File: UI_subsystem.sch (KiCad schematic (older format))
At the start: 19 parts

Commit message: Added UI buttons, LEDs, Decoupling caps, MCU connections, and other good stuff.
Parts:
- added R?: 100, symbol Device:R_US
- added ZNP_BTN_?: SW_Push, symbol Switch:SW_Push
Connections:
- net labels added: GND, MCU_RESET, MCU_VDD
- net labels removed: +3V3, 3.3_TFT, GND8, PWR_LED
- wire segments 50 -> 57
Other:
- moved on the sheet: BB_BTN_301, BB_BTN_302, LED301, LED302, PWR301, R301, R302, R303, R304, R305, R306, R307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

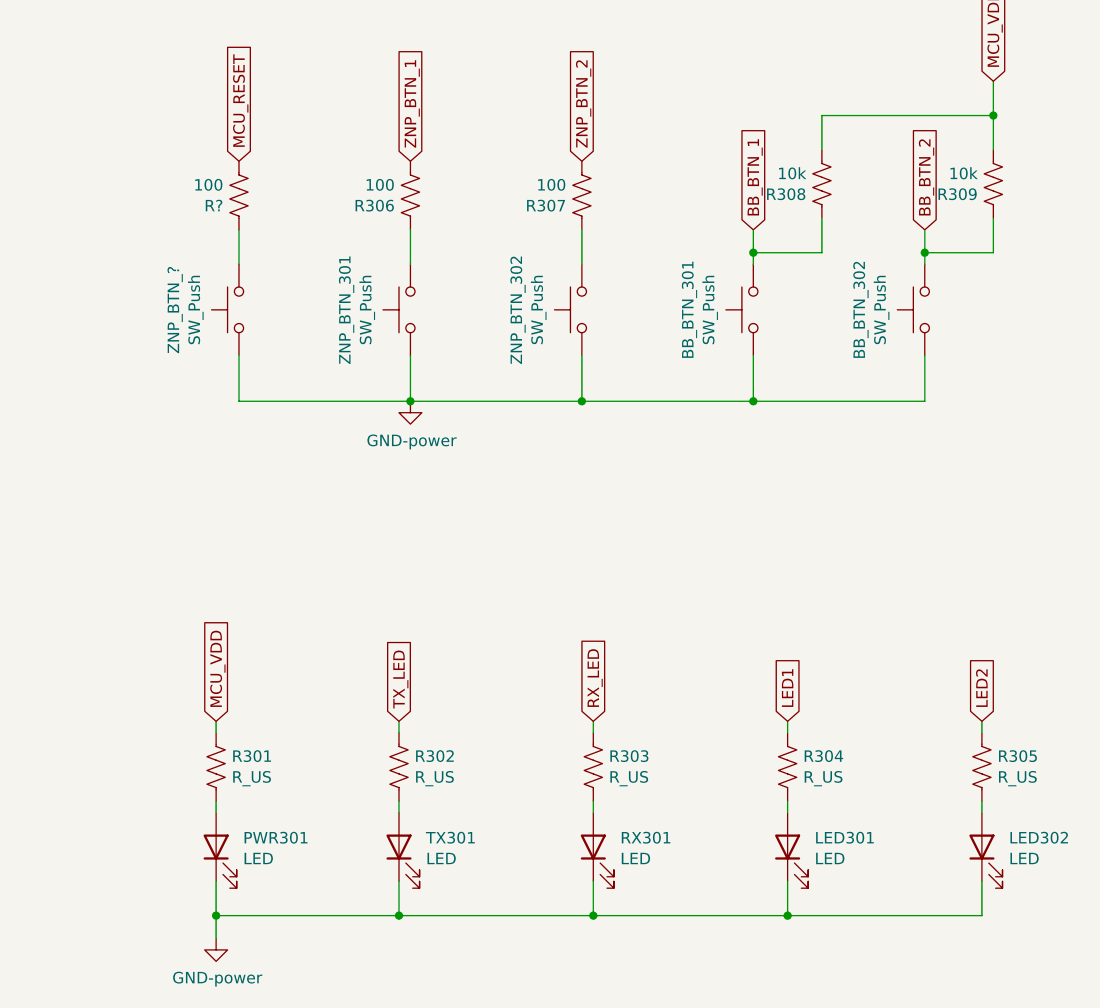
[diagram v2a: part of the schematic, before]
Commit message: Finished Adding MCU connections and combined crystal and MCU sheets.
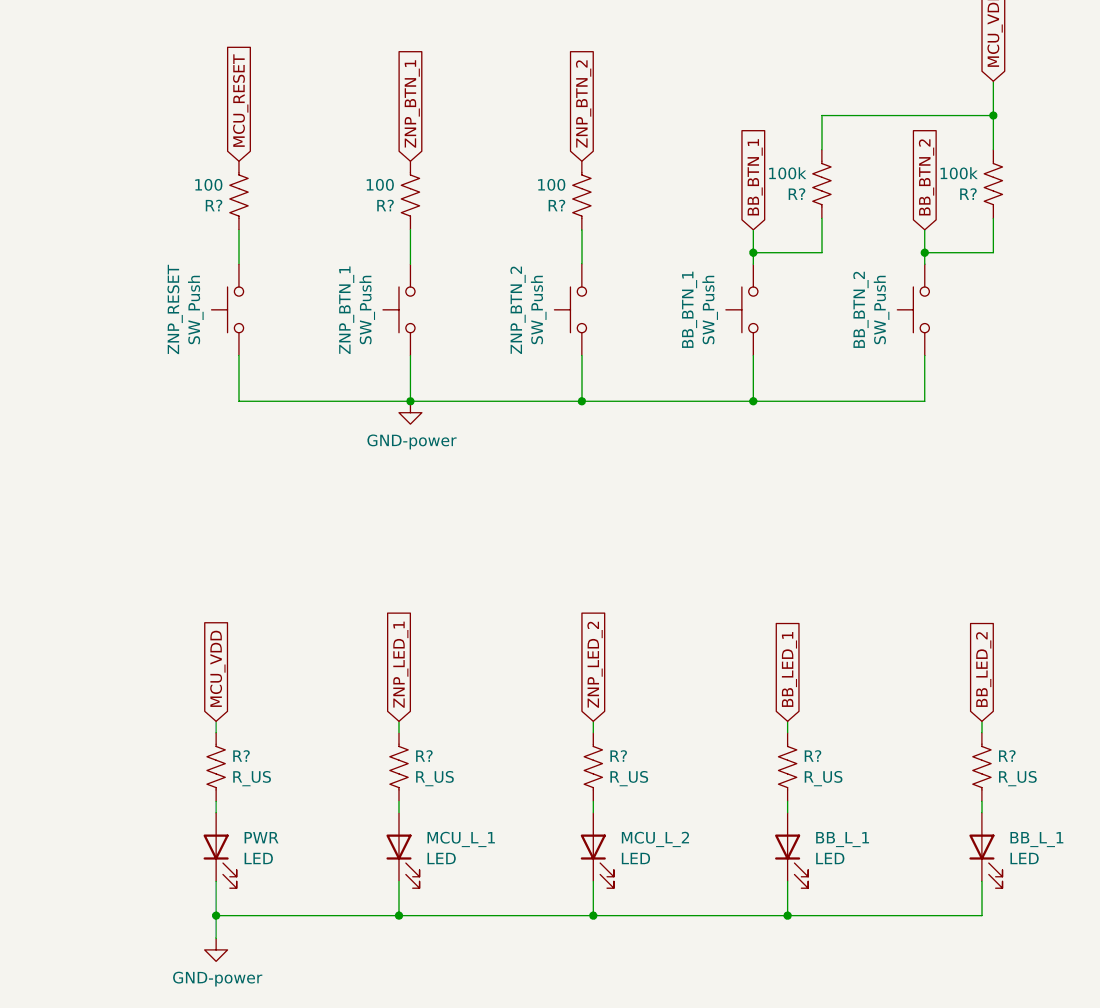
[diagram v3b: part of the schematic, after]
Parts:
- R?: renamed from R308; value 10k -> 100k
- R?: renamed from R309; value 10k -> 100k
- gave numbers to parts that had none: 1
- renumbered BB_BTN_301 to BB_BTN_1, BB_BTN_302 to BB_BTN_2, LED301 to BB_L_1, LED302 to BB_L_1, TX301 to MCU_L_1, RX301 to MCU_L_2, PWR301 to PWR, R301 to R?, R302 to R?, R303 to R?, R304 to R?, R305 to R?, R306 to R?, R307 to R?, ZNP_BTN_301 to ZNP_BTN_1, ZNP_BTN_302 to ZNP_BTN_2
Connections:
- net LED1 renamed BB_LED_1
- net LED2 renamed BB_LED_2
- net RX_LED renamed ZNP_LED_2
- net TX_LED renamed ZNP_LED_1
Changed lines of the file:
@@
 $Descr A4 11693 8268
 encoding utf-8
-Sheet 3 7
+Sheet 3 6
 Title ""
 Date ""
@@
 	3150 3550 3300 3550
 $Comp
-L Switch:SW_Push ZNP_BTN_301
+L Switch:SW_Push ZNP_BTN_1
 U 1 1 614536C0
 P 7650 2450
-F 0 "ZNP_BTN_301" H 7650 2735 50  0000 C CNN
+F 0 "ZNP_BTN_1" H 7650 2735 50  0000 C CNN
 F 1 "SW_Push" H 7650 2644 50  0000 C CNN
 F 2 "" H 7650 2650 50  0001 C CNN
@@
 $EndComp
 $Comp
-L Switch:SW_Push ZNP_BTN_302
+L Switch:SW_Push ZNP_BTN_2
 U 1 1 614542E2
 P 8400 2450
-F 0 "ZNP_BTN_302" H 8400 2735 50  0000 C CNN
+F 0 "ZNP_BTN_2" H 8400 2735 50  0000 C CNN
 F 1 "SW_Push" H 8400 2644 50  0000 C CNN
 F 2 "" H 8400 2650 50  0001 C CNN
@@
 $EndComp
 $Comp
-L Switch:SW_Push BB_BTN_301
+L Switch:SW_Push BB_BTN_1
 U 1 1 614544C6
 P 9150 2450
-F 0 "BB_BTN_301" H 9150 2735 50  0000 C CNN
+F 0 "BB_BTN_1" H 9150 2735 50  0000 C CNN
 F 1 "SW_Push" H 9150 2644 50  0000 C CNN
 F 2 "" H 9150 2650 50  0001 C CNN
@@
 $EndComp
 $Comp
-L Switch:SW_Push BB_BTN_302
+L Switch:SW_Push BB_BTN_2
 U 1 1 61454891
 P 9900 2450
-F 0 "BB_BTN_302" H 9900 2735 50  0000 C CNN
+F 0 "BB_BTN_2" H 9900 2735 50  0000 C CNN
 F 1 "SW_Push" H 9900 2644 50  0000 C CNN
 F 2 "" H 9900 2650 50  0001 C CNN
@@
 $EndComp
 $Comp
-L Device:LED PWR301
+L Device:LED PWR
 U 1 1 614557C3
 P 6800 4800
-F 0 "PWR301" V 6839 4682 50  0000 R CNN
+F 0 "PWR" V 6839 4682 50  0000 R CNN
 F 1 "LED" V 6748 4682 50  0000 R CNN
 F 2 "" H 6800 4800 50  0001 C CNN
@@
 $EndComp
 $Comp
-L Device:LED TX301
+L Device:LED MCU_L_1
 U 1 1 614568E7
 P 7600 4800
-F 0 "TX301" V 7639 4682 50  0000 R CNN
+F 0 "MCU_L_1" V 7639 4682 50  0000 R CNN
 F 1 "LED" V 7548 4682 50  0000 R CNN
 F 2 "" H 7600 4800 50  0001 C CNN
@@
 $EndComp
 $Comp
-L Device:LED RX301
+L Device:LED MCU_L_2
 U 1 1 61456F00
 P 8450 4800
-F 0 "RX301" V 8489 4682 50  0000 R CNN
+F 0 "MCU_L_2" V 8489 4682 50  0000 R CNN
 F 1 "LED" V 8398 4682 50  0000 R CNN
 F 2 "" H 8450 4800 50  0001 C CNN
@@
 $EndComp
 $Comp
-L Device:LED LED301
+L Device:LED BB_L_1
 U 1 1 614573C9
 P 9300 4800
-F 0 "LED301" V 9339 4682 50  0000 R CNN
+F 0 "BB_L_1" V 9339 4682 50  0000 R CNN
 F 1 "LED" V 9248 4682 50  0000 R CNN
 F 2 "" H 9300 4800 50  0001 C CNN
@@
 $EndComp
 $Comp
-L Device:LED LED302
+L Device:LED BB_L_1
 U 1 1 61457651
 P 10150 4800
-F 0 "LED302" V 10189 4682 50  0000 R CNN
+F 0 "BB_L_1" V 10189 4682 50  0000 R CNN
 F 1 "LED" V 10098 4682 50  0000 R CNN
 F 2 "" H 10150 4800 50  0001 C CNN
@@
 $EndComp
 $Comp
-L Device:R_US R301
+L Device:R_US R?
 U 1 1 614578E4
 P 6800 4450
-F 0 "R301" H 6868 4496 50  0000 L CNN
+F 0 "R?" H 6868 4496 50  0000 L CNN
 F 1 "R_US" H 6868 4405 50  0000 L CNN
 F 2 "" V 6840 4440 50  0001 C CNN
@@
 	6800 4950 6800 5100
 $Comp
-L Device:R_US R302
+L Device:R_US R?
 U 1 1 61463DB5
 P 7600 4450
-F 0 "R302" H 7668 4496 50  0000 L CNN
+F 0 "R?" H 7668 4496 50  0000 L CNN
 F 1 "R_US" H 7668 4405 50  0000 L CNN
 F 2 "" V 7640 4440 50  0001 C CNN
@@
 $EndComp
 $Comp
-L Device:R_US R303
+L Device:R_US R?
 U 1 1 614640E9
 P 8450 4450
-F 0 "R303" H 8518 4496 50  0000 L CNN
+F 0 "R?" H 8518 4496 50  0000 L CNN
 F 1 "R_US" H 8518 4405 50  0000 L CNN
 F 2 "" V 8490 4440 50  0001 C CNN
@@
 $EndComp
 $Comp
-L Device:R_US R304
+L Device:R_US R?
 U 1 1 614643AB
 P 9300 4450
-F 0 "R304" H 9368 4496 50  0000 L CNN
+F 0 "R?" H 9368 4496 50  0000 L CNN
 F 1 "R_US" H 9368 4405 50  0000 L CNN
 F 2 "" V 9340 4440 50  0001 C CNN
@@
 $EndComp
 $Comp
-L Device:R_US R305
+L Device:R_US R?
 U 1 1 61464797
 P 10150 4450
-F 0 "R305" H 10218 4496 50  0000 L CNN
+F 0 "R?" H 10218 4496 50  0000 L CNN
 F 1 "R_US" H 10218 4405 50  0000 L CNN
 F 2 "" V 10190 4440 50  0001 C CNN
@@
 Connection ~ 9300 5100
 Text GLabel 7600 4250 1    50   Input ~ 0
-TX_LED
+ZNP_LED_1
 Text GLabel 8450 4250 1    50   Input ~ 0
-RX_LED
+ZNP_LED_2
 Text GLabel 9300 4250 1    50   Input ~ 0
-LED1
+BB_LED_1
 Text GLabel 10150 4250 1    50   Input ~ 0
-LED2
+BB_LED_2
 Wire Wire Line
 	6800 4300 6800 4250
@@
 $EndComp
 $Comp
-L Device:R_US R306
+L Device:R_US R?
 U 1 1 61481C85
 P 7650 1950
-F 0 "R306" H 7718 1996 50  0000 L CNN
+F 0 "R?" H 7718 1996 50  0000 L CNN
 F 1 "100" H 7718 1905 50  0000 L CNN
 F 2 "" V 7690 1940 50  0001 C CNN
@@
 Connection ~ 10200 1600
 $Comp
-L Device:R_US R307
+L Device:R_US R?
 U 1 1 61482BE5
 P 8400 1950
-F 0 "R307" H 8468 1996 50  0000 L CNN
+F 0 "R?" H 8468 1996 50  0000 L CNN
 F 1 "100" H 8468 1905 50  0000 L CNN
 F 2 "" V 8440 1940 50  0001 C CNN
@@
 $EndComp
 $Comp
-L Device:R_US R308
+L Device:R_US R?
 U 1 1 614833DA
 P 9450 1900
-F 0 "R308" H 9518 1946 50  0000 L CNN
-F 1 "10k" H 9518 1855 50  0000 L CNN
+F 0 "R?" H 9518 1946 50  0000 L CNN
+F 1 "100k" H 9518 1855 50  0000 L CNN
 F 2 "" V 9490 1890 50  0001 C CNN
 F 3 "~" H 9450 1900 50  0001 C CNN
@@
 $EndComp
 $Comp
-L Device:R_US R309
+L Device:R_US R?
 U 1 1 614839E0
 P 10200 1900
-F 0 "R309" H 10268 1946 50  0000 L CNN
-F 1 "10k" H 10268 1855 50  0000 L CNN
+F 0 "R?" H 10268 1946 50  0000 L CNN
+F 1 "100k" H 10268 1855 50  0000 L CNN
 F 2 "" V 10240 1890 50  0001 C CNN
 F 3 "~" H 10200 1900 50  0001 C CNN
@@
 	10200 1450 10200 1600
 $Comp
-L Switch:SW_Push ZNP_BTN_?
+L Switch:SW_Push ZNP_RESET
 U 1 1 614AD723
 P 6900 2450
-F 0 "ZNP_BTN_?" H 6900 2735 50  0000 C CNN
+F 0 "ZNP_RESET" H 6900 2735 50  0000 C CNN
 F 1 "SW_Push" H 6900 2644 50  0000 C CNN
 F 2 "" H 6900 2650 50  0001 C CNN

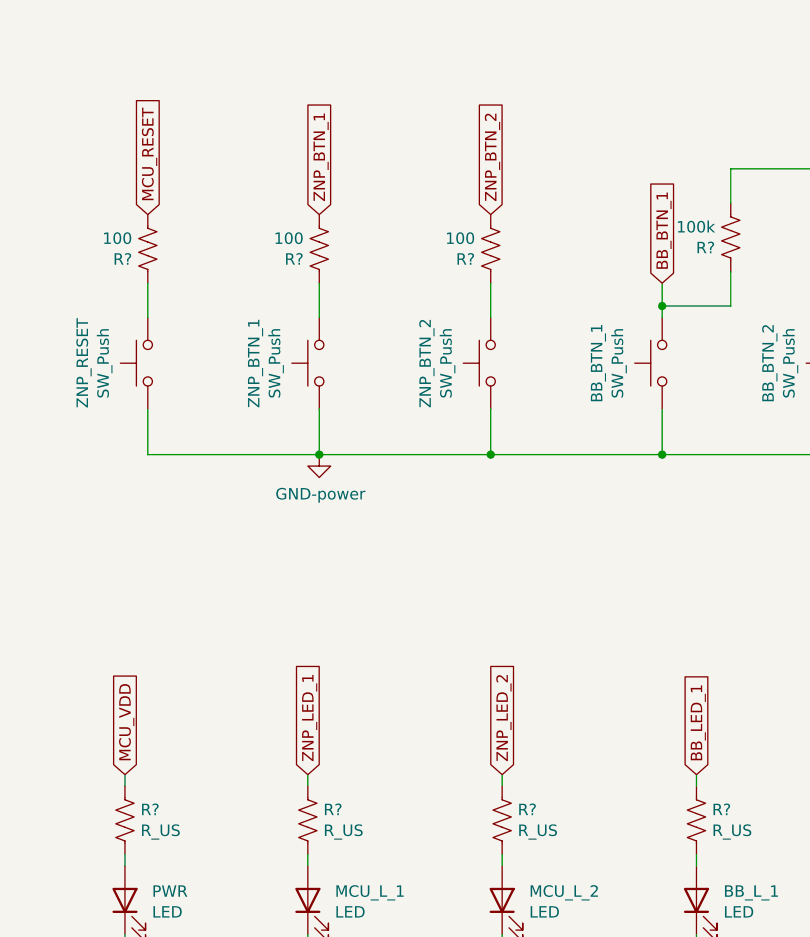
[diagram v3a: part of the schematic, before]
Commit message: Fixed some Global labels.
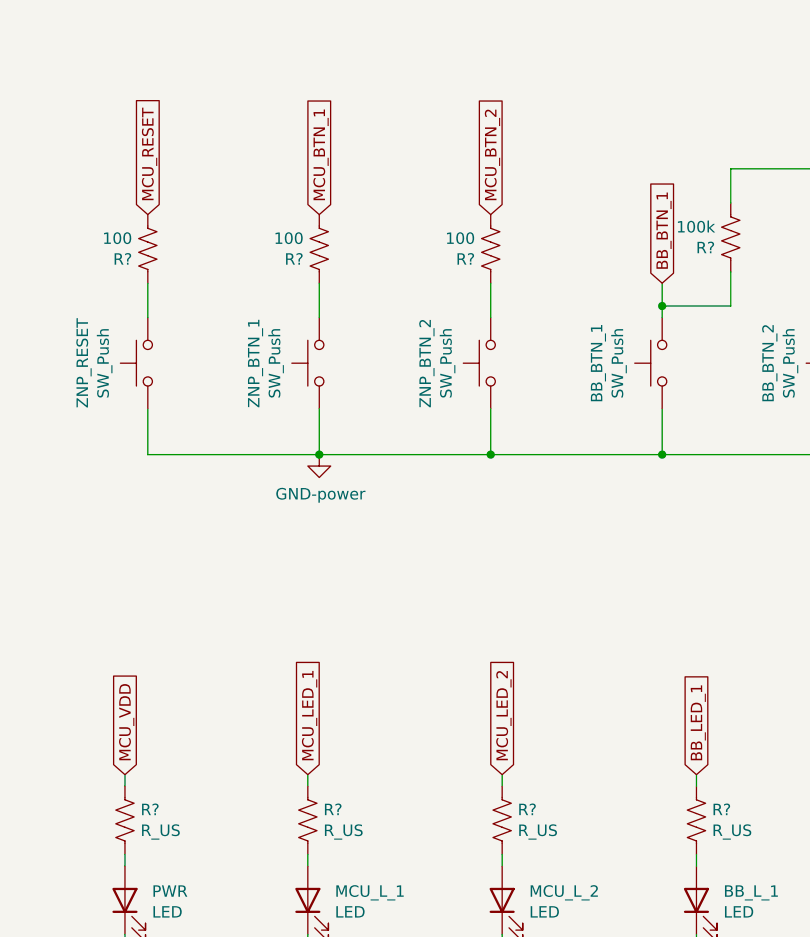
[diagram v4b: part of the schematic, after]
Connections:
- net ZNP_BTN_1 renamed MCU_BTN_1
- net ZNP_BTN_2 renamed MCU_BTN_2
- net ZNP_LED_1 renamed MCU_LED_1
- net ZNP_LED_2 renamed MCU_LED_2
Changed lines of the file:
@@
 Connection ~ 9300 5100
 Text GLabel 7600 4250 1    50   Input ~ 0
-ZNP_LED_1
+MCU_LED_1
 Text GLabel 8450 4250 1    50   Input ~ 0
-ZNP_LED_2
+MCU_LED_2
 Text GLabel 9300 4250 1    50   Input ~ 0
 BB_LED_1
@@
 $EndComp
 Text GLabel 7650 1800 1    50   Input ~ 0
-ZNP_BTN_1
+MCU_BTN_1
 Wire Wire Line
 	7650 2650 7650 2850
@@
 	9900 2650 9900 2850
 Text GLabel 8400 1800 1    50   Input ~ 0
-ZNP_BTN_2
+MCU_BTN_2
 Text GLabel 9150 2100 1    50   Input ~ 0
 BB_BTN_1
